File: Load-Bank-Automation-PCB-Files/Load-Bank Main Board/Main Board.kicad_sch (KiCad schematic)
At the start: 4 parts

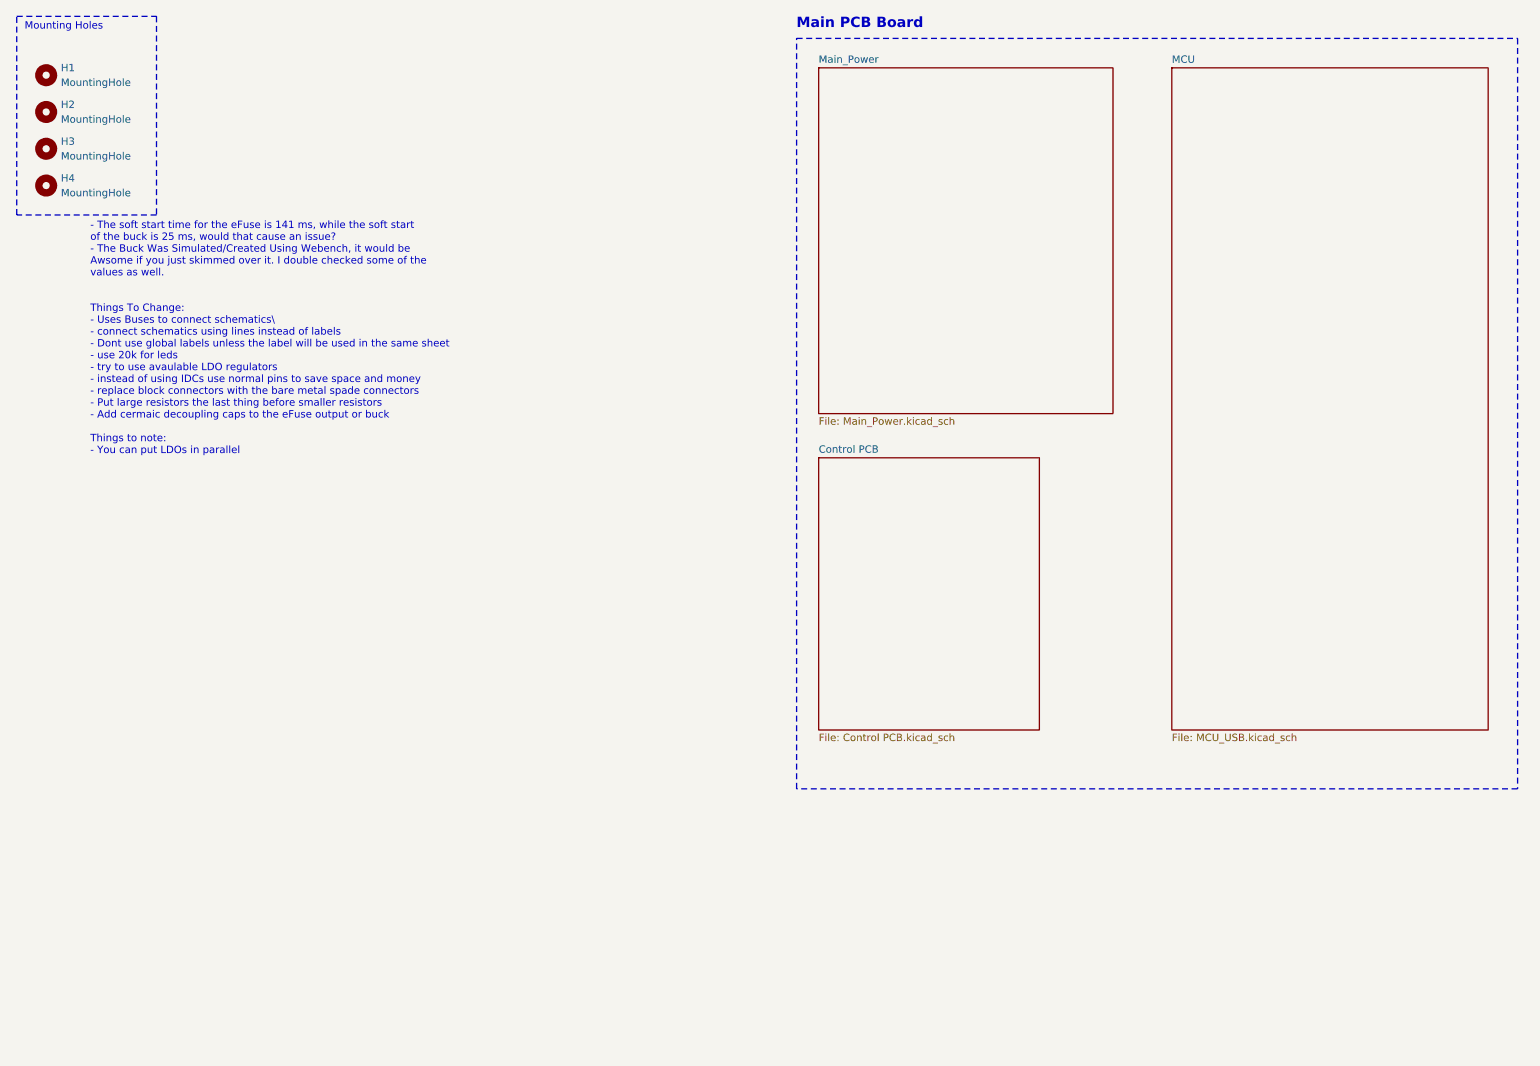
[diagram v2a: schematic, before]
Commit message: All footprints assigned and new schematic changes
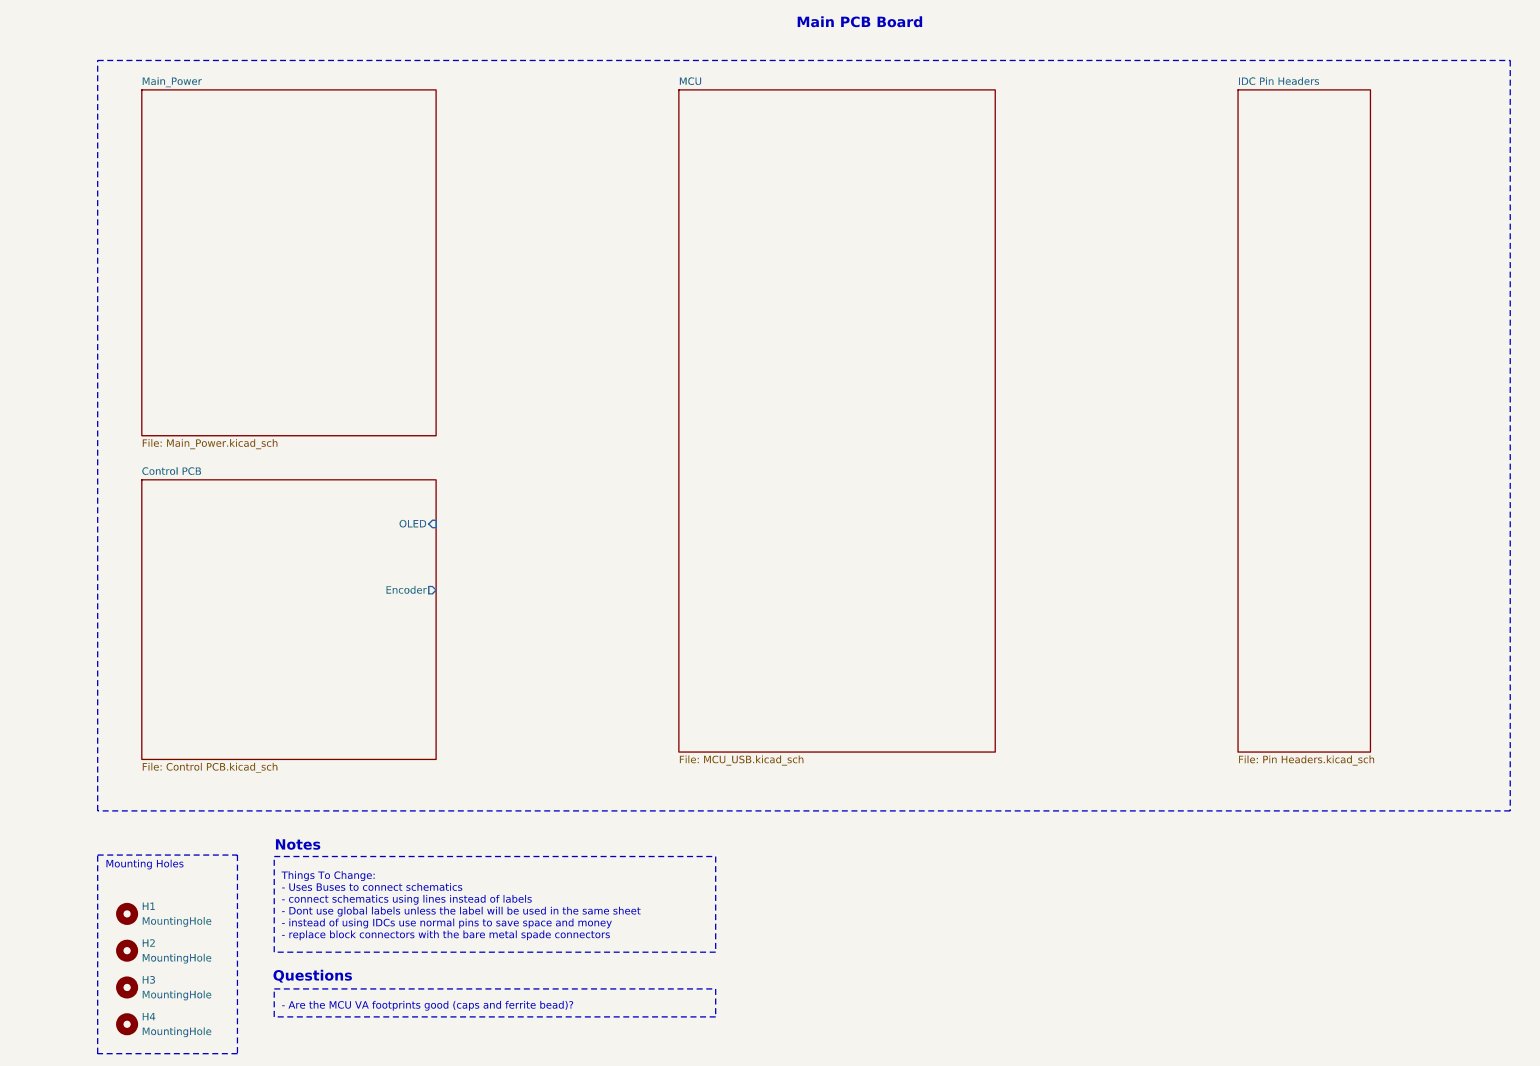
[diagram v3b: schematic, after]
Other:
- added sheet IDC Pin Headers (Pin Headers.kicad_sch)
- sheet Control PCB ports: added Encoder, OLED; removed none
- note added: "- Are the MCU VA footprints good (caps and ferrite bead)?"
- note added: "Notes"
- note added: "Questions"
- note added: "Things To Change: - Uses Buses to connect schematics - connect schematics using lines instead of labels - Dont use global labels unless the label will be used in the same sheet - instead of using IDCs use normal pins to save space and money - replace block connectors with the bare metal spade connectors"
- note removed: "- The soft start time for the eFuse is 141 ms, while the soft start of the buck is 25 ms, would that cause an issue? - The Buck Was Simulated/Created Using Webench, it would be Awsome if you just skimmed over it. I double checked some of the values as well. Things To Change: - Uses Buses to connect schematics\ - connect schematics using lines instead of labels - Dont use global labels unless the 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"
- moved on the sheet: H1, H2, H3, H4
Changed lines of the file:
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@@
 	(paper "A4")
 	(rectangle
-		(start 15.24 15.24)
-		(end 39.37 49.53)
+		(start 59.69 183.134)
+		(end 135.89 187.96)
 		(stroke
 			(width 0)
+			(type dash)
+		)
+		(fill
+			(type none)
+		)
+	)
+	(rectangle
+		(start 59.69 160.274)
+		(end 135.89 176.784)
+		(stroke
+			(width 0)
+			(type dash)
+		)
+		(fill
+			(type none)
+		)
+	)
+	(rectangle
+		(start 29.21 160.02)
+		(end 53.34 194.31)
+		(stroke
+			(width 0.2032)
 			(type dot)
 		)
@@
 	)
 	(rectangle
-		(start 149.86 19.05)
-		(end 274.32 148.59)
-		(stroke
-			(width 0)
+		(start 29.21 22.86)
+		(end 273.05 152.4)
+		(stroke
+			(width 0.2032)
 			(type dot)
 		)
@@
 		)
 	)
-	(text "- The soft start time for the eFuse is 141 ms, while the soft start \nof the buck is 25 ms, would that cause an issue?\n- The Buck Was Simulated/Created Using Webench, it would be \nAwsome if you just skimmed over it. I double checked some of the \nvalues as well.\n\n\nThings To Change:\n- Uses Buses to connect schematics\\\n- connect schematics using lines instead of labels\n- Dont use global labels unless the label will be used in the same sheet\n- use 20k for leds\n- try to use avaulable LDO regulators\n- instead of using IDCs use normal pins to save space and money\n- replace block connectors with the bare metal spade connectors\n- Put large resistors the last thing before smaller resistors \n- Add cermaic decoupling caps to the eFuse output or buck\n\nThings to note:\n- You can put LDOs in parallel"
-		(exclude_from_sim no)
-		(at 27.94 70.866 0)
+	(text "Things To Change:\n- Uses Buses to connect schematics\n- connect schematics using lines instead of labels\n- Dont use global labels unless the label will be used in the same sheet\n- instead of using IDCs use normal pins to save space and money\n- replace block connectors with the bare metal spade connectors"
+		(exclude_from_sim no)
+		(at 60.96 168.91 0)
 		(effects
 			(font
@@
 	(text "Mounting Holes"
 		(exclude_from_sim no)
-		(at 23.368 17.018 0)
+		(at 37.338 161.798 0)
 		(effects
 			(font
@@
 		)
 	)
+	(text "Questions"
+		(exclude_from_sim no)
+		(at 59.436 181.102 0)
+		(effects
+			(font
+				(size 1.778 1.778)
+				(thickness 0.254)
+				(bold yes)
+			)
+			(justify left)
+		)
+	)
+	(text "Notes"
+		(exclude_from_sim no)
+		(at 63.754 158.496 0)
+		(effects
+			(font
+				(size 1.778 1.778)
+				(thickness 0.254)
+				(bold yes)
+			)
+		)
+	)
+	(text "- Are the MCU VA footprints good (caps and ferrite bead)?"
+		(exclude_from_sim no)
+		(at 60.96 186.182 0)
+		(effects
+			(font
+				(size 1.27 1.27)
+			)
+			(justify left)
+		)
+	)
 	(symbol
 		(lib_id "Mechanical:MountingHole")
-		(at 20.32 25.4 0)
+		(at 34.29 170.18 0)
 		(unit 1)
 		(exclude_from_sim no)
@@
 		(fields_autoplaced yes)
 		(property "Reference" "H1"
-			(at 22.86 24.1299 0)
+			(at 36.83 168.9099 0)
 			(effects
 				(font
@@
 		)
 		(property "Value" "MountingHole"
-			(at 22.86 26.6699 0)
+			(at 36.83 171.4499 0)
 			(effects
 				(font
@@
 		)
 		(property "Footprint" "MountingHole:MountingHole_3.2mm_M3"
-			(at 20.32 25.4 0)
+			(at 34.29 170.18 0)
 			(effects
 				(font
@@
 		)
 		(property "Datasheet" "~"
-			(at 20.32 25.4 0)
+			(at 34.29 170.18 0)
 			(effects
 				(font
@@
 		)
 		(property "Description" "Mounting Hole without connection"
-			(at 20.32 25.4 0)
+			(at 34.29 170.18 0)
 			(effects
 				(font
@@
 	(symbol
 		(lib_id "Mechanical:MountingHole")
-		(at 20.32 31.75 0)
+		(at 34.29 176.53 0)
 		(unit 1)
 		(exclude_from_sim no)
@@
 		(fields_autoplaced yes)
 		(property "Reference" "H2"
-			(at 22.86 30.4799 0)
+			(at 36.83 175.2599 0)
 			(effects
 				(font
@@
 		)
 		(property "Value" "MountingHole"
-			(at 22.86 33.0199 0)
+			(at 36.83 177.7999 0)
 			(effects
 				(font
@@
 		)
 		(property "Footprint" "MountingHole:MountingHole_3.2mm_M3"
-			(at 20.32 31.75 0)
+			(at 34.29 176.53 0)
 			(effects
 				(font
@@
 		)
 		(property "Datasheet" "~"
-			(at 20.32 31.75 0)
+			(at 34.29 176.53 0)
 			(effects
 				(font
@@
 		)
 		(property "Description" "Mounting Hole without connection"
-			(at 20.32 31.75 0)
+			(at 34.29 176.53 0)
 			(effects
 				(font
@@
 	(symbol
 		(lib_id "Mechanical:MountingHole")
-		(at 20.32 38.1 0)
+		(at 34.29 182.88 0)
 		(unit 1)
 		(exclude_from_sim no)
@@
 		(fields_autoplaced yes)
 		(property "Reference" "H3"
-			(at 22.86 36.8299 0)
+			(at 36.83 181.6099 0)
 			(effects
 				(font
@@
 		)
 		(property "Value" "MountingHole"
-			(at 22.86 39.3699 0)
+			(at 36.83 184.1499 0)
 			(effects
 				(font
@@
 		)
 		(property "Footprint" "MountingHole:MountingHole_3.2mm_M3"
-			(at 20.32 38.1 0)
+			(at 34.29 182.88 0)
 			(effects
 				(font
@@
 		)
 		(property "Datasheet" "~"
-			(at 20.32 38.1 0)
+			(at 34.29 182.88 0)
 			(effects
 				(font
@@
 		)
 		(property "Description" "Mounting Hole without connection"
-			(at 20.32 38.1 0)
+			(at 34.29 182.88 0)
 			(effects
 				(font
@@
 	(symbol
 		(lib_id "Mechanical:MountingHole")
-		(at 20.32 44.45 0)
+		(at 34.29 189.23 0)
 		(unit 1)
 		(exclude_from_sim no)
@@
 		(fields_autoplaced yes)
 		(property "Reference" "H4"
-			(at 22.86 43.1799 0)
+			(at 36.83 187.9599 0)
 			(effects
 				(font
@@
 		)
 		(property "Value" "MountingHole"
-			(at 22.86 45.7199 0)
+			(at 36.83 190.4999 0)
 			(effects
 				(font
@@
 		)
 		(property "Footprint" "MountingHole:MountingHole_3.2mm_M3"
-			(at 20.32 44.45 0)
+			(at 34.29 189.23 0)
 			(effects
 				(font
@@
 		)
 		(property "Datasheet" "~"
-			(at 20.32 44.45 0)
+			(at 34.29 189.23 0)
 			(effects
 				(font
@@
 		)
 		(property "Description" "Mounting Hole without connection"
-			(at 20.32 44.45 0)
+			(at 34.29 189.23 0)
 			(effects
 				(font
@@
 	)
 	(sheet
-		(at 153.67 91.44)
-		(size 38.1 46.99)
+		(at 226.06 27.94)
+		(size 22.86 114.3)
 		(exclude_from_sim no)
 		(in_bom yes)
@@
 		)
 		(fill
-			(color 0 0 0 0.0000)
-		)
-		(property "Sheetname" "Control PCB"
-			(at 153.67 90.7284 0)
+			(color 255 255 194 1.0000)
+		)
+		(property "Sheetname" "IDC Pin Headers"
+			(at 226.06 27.2284 0)
 			(effects
 				(font
@@
 			)
 		)
-		(property "Sheetfile" "Control PCB.kicad_sch"
-			(at 153.67 139.0146 0)
+		(property "Sheetfile" "Pin Headers.kicad_sch"
+			(at 226.06 142.8246 0)
 			(effects
 				(font
@@
 			(project "Main Board"
 				(path "/c82c4769-33eb-46b7-8d07-39045014a3da"
-					(page "6")
+					(page "7")
 				)
 			)
@@
 	)
 	(sheet
-		(at 214.63 24.13)
-		(size 54.61 114.3)
+		(at 36.83 95.25)
+		(size 50.8 48.26)
 		(exclude_from_sim no)
 		(in_bom yes)
@@
 		)
 		(fill
-			(color 0 0 0 0.0000)
-		)
-		(property "Sheetname" "MCU"
-			(at 214.63 23.4184 0)
+			(color 255 255 194 1.0000)
+		)
+		(property "Sheetname" "Control PCB"
+			(at 36.83 94.5384 0)
 			(effects
 				(font
@@
 			)
 		)
-		(property "Sheetfile" "MCU_USB.kicad_sch"
-			(at 214.63 139.0146 0)
+		(property "Sheetfile" "Control PCB.kicad_sch"
+			(at 36.83 144.0946 0)
 			(effects
 				(font
@@
 			)
 		)
+		(pin "OLED" input
+			(at 87.63 102.87 0)
+			(effects
+				(font
+					(size 1.27 1.27)
+				)
+				(justify right)
+			)
+		)
+		(pin "Encoder" output
+			(at 87.63 114.3 0)
+			(effects
+				(font
+					(size 1.27 1.27)
+				)
+				(justify right)
+			)
+		)
 		(instances
 			(project "Main Board"
 				(path "/c82c4769-33eb-46b7-8d07-39045014a3da"
-					(page "3")
+					(page "6")
 				)
 			)
@@
 	)
 	(sheet
-		(at 153.67 24.13)
-		(size 50.8 59.69)
+		(at 129.54 27.94)
+		(size 54.61 114.3)
 		(exclude_from_sim no)
 		(in_bom yes)
@@
 		)
 		(fill
-			(color 255 229 191 1.0000)
+			(color 255 255 194 1.0000)
+		)
+		(property "Sheetname" "MCU"
+			(at 129.54 27.2284 0)
+			(effects
+				(font
+					(size 1.27 1.27)
+				)
+				(justify left bottom)
+			)
+		)
+		(property "Sheetfile" "MCU_USB.kicad_sch"
+			(at 129.54 142.8246 0)
+			(effects
+				(font
+					(size 1.27 1.27)
+				)
+				(justify left top)
+			)
+		)
+		(instances
+			(project "Main Board"
+				(path "/c82c4769-33eb-46b7-8d07-39045014a3da"
+					(page "3")
+				)
+			)
+		)
+	)
+	(sheet
+		(at 36.83 27.94)
+		(size 50.8 59.69)
+		(exclude_from_sim no)
+		(in_bom yes)
+		(on_board yes)
+		(dnp no)
+		(fields_autoplaced yes)
+		(stroke
+			(width 0.1524)
+			(type solid)
+		)
+		(fill
+			(color 255 255 194 1.0000)
 		)
 		(property "Sheetname" "Main_Power"
-			(at 153.67 23.4184 0)
+			(at 36.83 27.2284 0)
 			(effects
 				(font
@@
 		)
 		(property "Sheetfile" "Main_Power.kicad_sch"
-			(at 153.67 84.4046 0)
-			(effects
-				(font
+			(at 36.83 88.2146 0)
+			(effects
+				(font

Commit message: Clearing up electrical rule errors
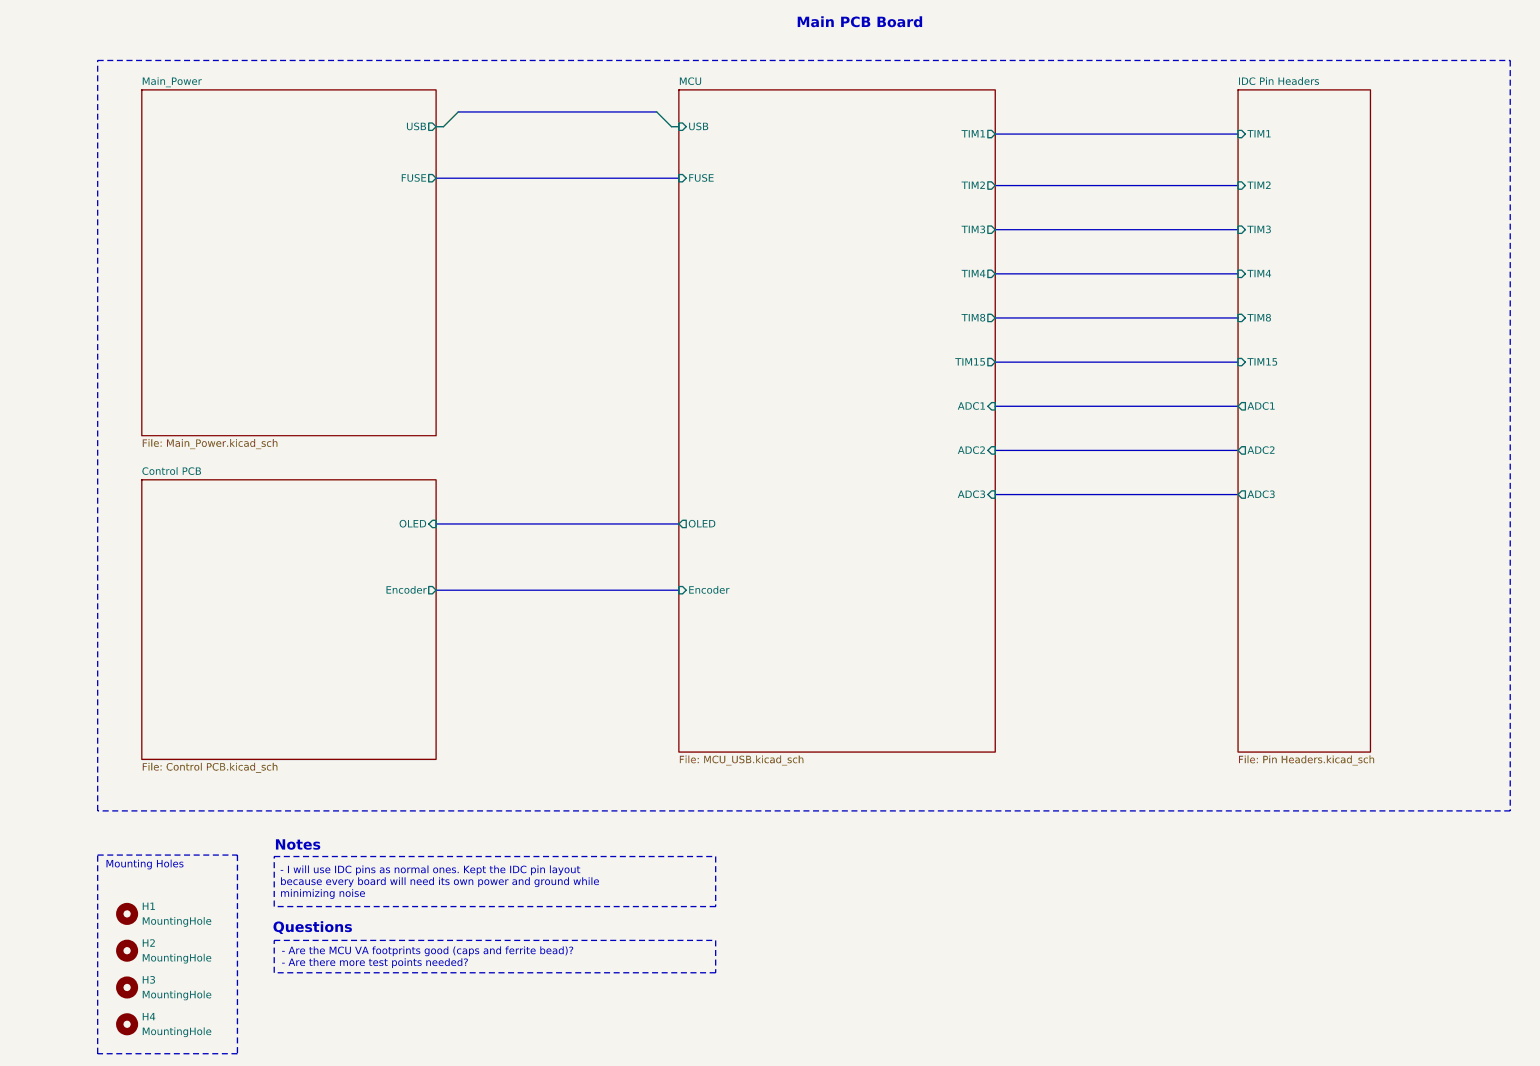
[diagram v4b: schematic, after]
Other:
- sheet IDC Pin Headers ports: added ADC1, ADC2, ADC3, TIM1, TIM15, TIM2, TIM3, TIM4, TIM8; removed none
- sheet MCU ports: added ADC1, ADC2, ADC3, Encoder, FUSE, OLED, TIM1, TIM15, TIM2, TIM3, TIM4, TIM8, USB; removed none
- sheet Main_Power ports: added FUSE, USB; removed none
- note added: "- Are the MCU VA footprints good (caps and ferrite bead)? - Are there more test points needed?"
- note added: "- I will use IDC pins as normal ones. Kept the IDC pin layout because every board will need its own power and ground while minimizing noise"
- note removed: "- Are the MCU VA footprints good (caps and ferrite bead)?"
- note removed: "Things To Change: - Uses Buses to connect schematics - connect schematics using lines instead of labels - Dont use global labels unless the label will be used in the same sheet - instead of using IDCs use normal pins to save space and money - replace block connectors with the bare metal spade connectors"
